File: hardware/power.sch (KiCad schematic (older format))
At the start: 51 parts, among them P1 CONN_01X02, Q1 DMG4712SSS, SW1 SPST, U7 LT3471, U8 PDM1-S

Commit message: Update sensors, hbridge caps, add heatsink
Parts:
- removed Q?: Q_NMOS_GDS, symbol Q_NMOS_GDS
- added C59: 1u, Capacitors_SMD:C_1206, symbol C
- added Q2: DMG4712SSS, symbol Q_NMOS_GDS
- added R42: 10k, symbol R
- C10, C11, C12, C7, C8, C9: footprint (none) -> Capacitors_SMD:C_0603
- C13, C14, C16, C4, C47, C48, C49: renamed from C?; footprint (none) -> Capacitors_SMD:C_0603
- C15: renamed from C?; footprint (none) -> Capacitors_SMD:C_1206
- C50: renamed from C?; value 10u -> 100n; footprint (none) -> Capacitors_SMD:C_1206
- R41: renamed from R?; value 10 -> 100
- gave numbers to parts that had none: 15
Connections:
- wire segments 123 -> 126

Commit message: Layout first draft
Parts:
- removed Q1, Q2: DMG4712SSS, symbol Q_NMOS_GDS
- added Q1, Q2: DMG4712SSS, Housings_SOIC:SOIC-8_3.9x4.9mm_Pitch1.27mm, symbol NMOS_8PIN
- R15: footprint (none) -> Resistors_SMD:R_0603
- U10: footprint (none) -> TO_SOT_Packages_SMD:TO-252-2Lead
- U16: footprint (none) -> TO_SOT_Packages_SMD:SOT-23-6
- U17, U9: footprint (none) -> TO_SOT_Packages_SMD:SOT-23-5
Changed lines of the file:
@@
-$EndComp
-$Comp
-L Q_NMOS_GDS Q1
-U 1 1 5987023F
-P 2100 7200
-F 0 "Q1" V 2100 7450 50  0000 R CNN
-F 1 "DMG4712SSS" V 2300 7450 50  0000 R CNN
-F 2 "" H 2300 7300 50  0001 C CNN
-F 3 "" H 2100 7200 50  0000 C CNN
-	1    2100 7200
-	0    -1   1    0
 $EndComp
 $Comp
@@
 F 0 "U16" H 6250 1500 60  0000 C CNN
 F 1 "MCP1501T-30E" H 6250 2050 60  0000 C CNN
-F 2 "" H 6200 1750 60  0001 C CNN
+F 2 "TO_SOT_Packages_SMD:SOT-23-6" H 6200 1750 60  0001 C CNN
 F 3 "" H 6200 1750 60  0000 C CNN
 	1    6250 1800
@@
 F 0 "U10" H 3800 1550 60  0000 C CNN
 F 1 "LF33ABDT" H 3650 1950 60  0000 C CNN
-F 2 "" H 3600 1600 60  0001 C CNN
+F 2 "TO_SOT_Packages_SMD:TO-252-2Lead" H 3600 1600 60  0001 C CNN
 F 3 "" H 3600 1600 60  0000 C CNN
 	1    3650 1750
@@
 F 0 "R15" V 2630 5850 50  0000 C CNN
 F 1 "10k" V 2550 5850 50  0000 C CNN
-F 2 "" V 2480 5850 50  0001 C CNN
+F 2 "Resistors_SMD:R_0603" V 2480 5850 50  0001 C CNN
 F 3 "" H 2550 5850 50  0000 C CNN
 	1    2550 5850
@@
 F 0 "U17" H 9250 4750 60  0000 C CNN
 F 1 "MIC5225-5.0" H 9300 5250 60  0000 C CNN
-F 2 "" H 9250 5000 60  0001 C CNN
+F 2 "TO_SOT_Packages_SMD:SOT-23-5" H 9250 5000 60  0001 C CNN
 F 3 "" H 9250 5000 60  0000 C CNN
 	1    9250 5000
@@
 F 0 "U9" H 3150 3050 60  0000 C CNN
 F 1 "MIC5225-5.0" H 3200 3550 60  0000 C CNN
-F 2 "" H 3150 3300 60  0001 C CNN
+F 2 "TO_SOT_Packages_SMD:SOT-23-5" H 3150 3300 60  0001 C CNN
 F 3 "" H 3150 3300 60  0000 C CNN
 	1    3150 3300
@@
 	9450 2000 9100 2000
 $Comp
-L Q_NMOS_GDS Q2
-U 1 1 59CA6F7C
-P 10050 2000
-F 0 "Q2" H 10300 2000 50  0000 R CNN
-F 1 "DMG4712SSS" H 10700 1900 50  0000 R CNN
-F 2 "" H 10250 2100 50  0001 C CNN
-F 3 "" H 10050 2000 50  0000 C CNN
-	1    10050 2000
-	1    0    0    -1
-$EndComp
-$Comp
 L R R42
 U 1 1 59CA88AD
@@
 	11000 2350 11000 1900
 Connection ~ 10750 2350
+$Comp
+L NMOS_8PIN Q2
+U 1 1 59BD8B92
+P 10050 2000
+F 0 "Q2" H 10350 2050 50  0000 R CNN
+F 1 "DMG4712SSS" H 10700 1950 50  0000 R CNN
+F 2 "Housings_SOIC:SOIC-8_3.9x4.9mm_Pitch1.27mm" H 10250 2100 50  0001 C CNN
+F 3 "" H 10050 2000 50  0000 C CNN
+	1    10050 2000
+	1    0    0    -1
+$EndComp
+$Comp
+L NMOS_8PIN Q1
+U 1 1 59BDA6D3
+P 2100 7200
+F 0 "Q1" V 2100 7450 50  0000 R CNN
+F 1 "DMG4712SSS" V 2350 7400 50  0000 R CNN
+F 2 "Housings_SOIC:SOIC-8_3.9x4.9mm_Pitch1.27mm" H 2300 7300 50  0001 C CNN
+F 3 "" H 2100 7200 50  0000 C CNN
+	1    2100 7200
+	0    -1   1    0
+$EndComp
 $EndSCHEMATC

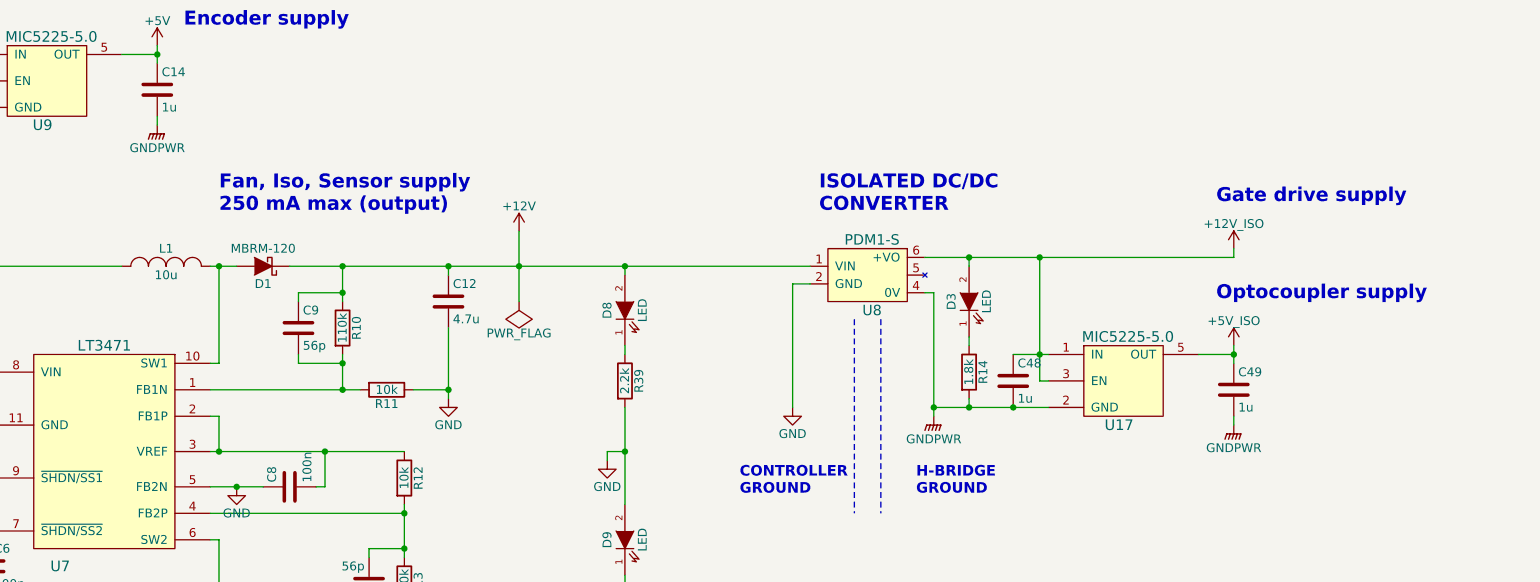
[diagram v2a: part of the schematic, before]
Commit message: revised power layout
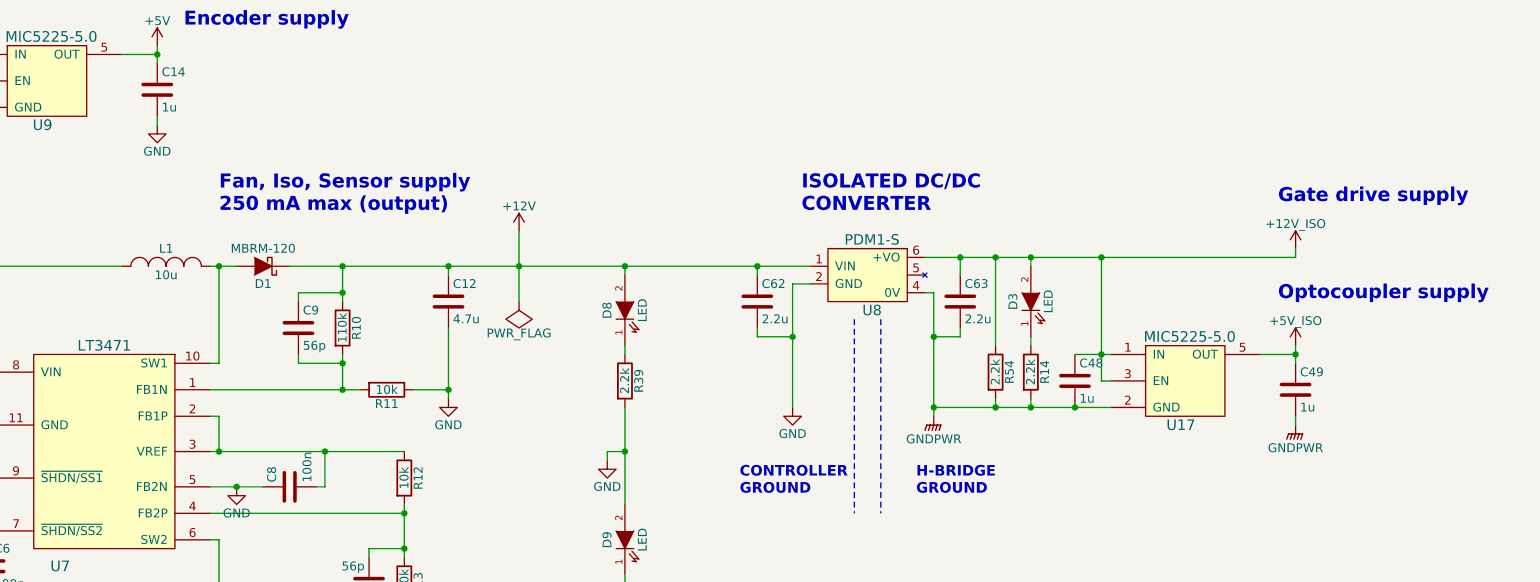
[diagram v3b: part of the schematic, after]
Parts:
- added C62, C63: 2.2u, symbol C
- added R54: 2.2k, symbol R
- R14: value 1.8k -> 2.2k
- U8: footprint (none) -> 2kwMotorController:PDM2-S
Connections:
- wire segments 126 -> 134
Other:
- moved on the sheet: C48, C49, D3, R14, U17
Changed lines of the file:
@@
 F 0 "U8" H 7850 4200 59  0000 C CNN
 F 1 "PDM1-S" H 7850 4600 59  0000 C CNN
-F 2 "" H 7850 4400 59  0001 C CNN
+F 2 "2kwMotorController:PDM2-S" H 7850 4400 59  0001 C CNN
 F 3 "" H 7850 4400 59  0000 C CNN
 	1    7800 4400
@@
 L R R14
 U 1 1 598583E6
-P 8400 4950
-F 0 "R14" V 8480 4950 50  0000 C CNN
-F 1 "1.8k" V 8400 4950 50  0000 C CNN
-F 2 "Resistors_SMD:R_0603" V 8330 4950 50  0001 C CNN
-F 3 "" H 8400 4950 50  0000 C CNN
-	1    8400 4950
+P 8750 4950
+F 0 "R14" V 8830 4950 50  0000 C CNN
+F 1 "2.2k" V 8750 4950 50  0000 C CNN
+F 2 "Resistors_SMD:R_0603" V 8680 4950 50  0001 C CNN
+F 3 "" H 8750 4950 50  0000 C CNN
+	1    8750 4950
 	1    0    0    -1
 $EndComp
@@
 L LED D3
 U 1 1 5985847D
-P 8400 4550
-F 0 "D3" H 8400 4650 50  0000 C CNN
-F 1 "LED" H 8400 4450 50  0000 C CNN
-F 2 "Diodes_SMD:SOD-123" H 8400 4550 50  0001 C CNN
-F 3 "" H 8400 4550 50  0000 C CNN
-	1    8400 4550
+P 8750 4550
+F 0 "D3" H 8750 4650 50  0000 C CNN
+F 1 "LED" H 8750 4450 50  0000 C CNN
+F 2 "Diodes_SMD:SOD-123" H 8750 4550 50  0001 C CNN
+F 3 "" H 8750 4550 50  0000 C CNN
+	1    8750 4550
 	0    -1   -1   0
 $EndComp
@@
 Text Notes 7100 5650 0    60   ~ 12
 CONTROLLER\nGROUND
-Text Notes 7550 4050 0    79   ~ 16
+Text Notes 7450 4050 0    79   ~ 16
 ISOLATED DC/DC\nCONVERTER
 $Comp
@@
 L +12V_ISO #PWR031
 U 1 1 59AAFB5D
-P 9900 4250
-F 0 "#PWR031" H 9900 4100 50  0001 C CNN
-F 1 "+12V_ISO" H 9900 4390 50  0000 C CNN
-F 2 "" H 9900 4250 50  0000 C CNN
-F 3 "" H 9900 4250 50  0000 C CNN
-	1    9900 4250
+P 10250 4250
+F 0 "#PWR031" H 10250 4100 50  0001 C CNN
+F 1 "+12V_ISO" H 10250 4390 50  0000 C CNN
+F 2 "" H 10250 4250 50  0000 C CNN
+F 3 "" H 10250 4250 50  0000 C CNN
+	1    10250 4250
 	1    0    0    -1
 $EndComp
@@
 L +5V_ISO #PWR041
 U 1 1 59B4088F
-P 9900 4800
-F 0 "#PWR041" H 9900 4650 50  0001 C CNN
-F 1 "+5V_ISO" H 9900 4940 50  0000 C CNN
-F 2 "" H 9900 4800 50  0000 C CNN
-F 3 "" H 9900 4800 50  0000 C CNN
-	1    9900 4800
+P 10250 4800
+F 0 "#PWR041" H 10250 4650 50  0001 C CNN
+F 1 "+5V_ISO" H 10250 4940 50  0000 C CNN
+F 2 "" H 10250 4800 50  0000 C CNN
+F 3 "" H 10250 4800 50  0000 C CNN
+	1    10250 4800
 	1    0    0    -1
 $EndComp
@@
 L GNDPWR #PWR042
 U 1 1 59B428AC
-P 9900 5250
-F 0 "#PWR042" H 9900 5050 50  0001 C CNN
-F 1 "GNDPWR" H 9900 5120 50  0000 C CNN
-F 2 "" H 9900 5200 50  0000 C CNN
-F 3 "" H 9900 5200 50  0000 C CNN
-	1    9900 5250
+P 10250 5250
+F 0 "#PWR042" H 10250 5050 50  0001 C CNN
+F 1 "GNDPWR" H 10250 5120 50  0000 C CNN
+F 2 "" H 10250 5200 50  0000 C CNN
+F 3 "" H 10250 5200 50  0000 C CNN
+	1    10250 5250
 	1    0    0    -1
 $EndComp
@@
 Text Notes 6650 6500 0    79   ~ 16
 Sensor supply\n60 mA max (output)
-Text Notes 9800 4550 0    79   ~ 16
+Text Notes 10150 4550 0    79   ~ 16
 Optocoupler supply
-Text Notes 9800 4000 0    79   ~ 16
+Text Notes 10150 4000 0    79   ~ 16
 Gate drive supply
 $Comp
@@
 L C C49
 U 1 1 59B42573
-P 9900 5050
-F 0 "C49" H 9925 5150 50  0000 L CNN
-F 1 "1u" H 9925 4950 50  0000 L CNN
-F 2 "Capacitors_SMD:C_0603" H 9938 4900 50  0001 C CNN
-F 3 "" H 9900 5050 50  0000 C CNN
-	1    9900 5050
+P 10250 5050
+F 0 "C49" H 10275 5150 50  0000 L CNN
+F 1 "1u" H 10275 4950 50  0000 L CNN
+F 2 "Capacitors_SMD:C_0603" H 10288 4900 50  0001 C CNN
+F 3 "" H 10250 5050 50  0000 C CNN
+	1    10250 5050
 	1    0    0    -1
 $EndComp
@@
 L C C48
 U 1 1 59BEDB92
-P 8650 5000
-F 0 "C48" H 8675 5100 50  0000 L CNN
-F 1 "1u" H 8675 4900 50  0000 L CNN
-F 2 "Capacitors_SMD:C_0603" H 8688 4850 50  0001 C CNN
-F 3 "" H 8650 5000 50  0000 C CNN
-	1    8650 5000
+P 9000 5000
+F 0 "C48" H 9025 5100 50  0000 L CNN
+F 1 "1u" H 9025 4900 50  0000 L CNN
+F 2 "Capacitors_SMD:C_0603" H 9038 4850 50  0001 C CNN
+F 3 "" H 9000 5000 50  0000 C CNN
+	1    9000 5000
 	1    0    0    -1
 $EndComp
@@
 L MIC5225-5.0 U17
 U 1 1 59BF0E85
-P 9250 5000
-F 0 "U17" H 9250 4750 60  0000 C CNN
-F 1 "MIC5225-5.0" H 9300 5250 60  0000 C CNN
-F 2 "TO_SOT_Packages_SMD:SOT-23-5" H 9250 5000 60  0001 C CNN
-F 3 "" H 9250 5000 60  0000 C CNN
-	1    9250 5000
-	1    0    0    -1
-$EndComp
-$Comp
-L GNDPWR #PWR045
-U 1 1 59BF2CFC
-P 3800 3550
-F 0 "#PWR045" H 3800 3350 50  0001 C CNN
-F 1 "GNDPWR" H 3800 3420 50  0000 C CNN
-F 2 "" H 3800 3500 50  0000 C CNN
-F 3 "" H 3800 3500 50  0000 C CNN
-	1    3800 3550
+P 9600 5000
+F 0 "U17" H 9600 4750 60  0000 C CNN
+F 1 "MIC5225-5.0" H 9650 5250 60  0000 C CNN
+F 2 "TO_SOT_Packages_SMD:SOT-23-5" H 9600 5000 60  0001 C CNN
+F 3 "" H 9600 5000 60  0000 C CNN
+	1    9600 5000
 	1    0    0    -1
 $EndComp
@@
 	2550 1350 2550 1250
 Wire Wire Line
-	8150 4300 9900 4300
-Connection ~ 8800 4300
+	8150 4300 10250 4300
+Connection ~ 9150 4300
 Wire Wire Line
 	8150 4500 8200 4500
@@
 	8200 4500 8200 5200
 Wire Wire Line
-	8400 4750 8400 4800
-Wire Wire Line
-	8400 5100 8400 5150
-Wire Wire Line
-	8200 5150 8850 5150
+	8750 4750 8750 4800
+Wire Wire Line
+	8750 5100 8750 5150
+Wire Wire Line
+	8200 5150 9200 5150
 Connection ~ 8200 5150
 Wire Wire Line
@@
 	7400 4450 7400 5150
 Wire Wire Line
-	8400 4350 8400 4300
-Connection ~ 8400 4300
+	8750 4350 8750 4300
+Connection ~ 8750 4300
 Wire Wire Line
 	1100 1450 1100 7350
@@
 Connection ~ 4250 5600
 Wire Wire Line
-	9900 4300 9900 4250
+	10250 4300 10250 4250
 Wire Wire Line
 	6700 1650 6950 1650
@@
 	5450 4400 5450 4350
 Wire Wire Line
-	8800 4300 8800 5000
-Wire Wire Line
-	8650 4850 8850 4850
-Wire Wire Line
-	8800 5000 8850 5000
-Connection ~ 8800 4850
-Connection ~ 8400 5150
-Wire Wire Line
-	9900 4800 9900 4900
-Wire Wire Line
-	9900 4850 9700 4850
-Wire Wire Line
-	9900 5250 9900 5200
-Connection ~ 9900 4850
+	9150 4300 9150 5000
+Wire Wire Line
+	9000 4850 9200 4850
+Wire Wire Line
+	9150 5000 9200 5000
+Connection ~ 9150 4850
+Connection ~ 8750 5150
+Wire Wire Line
+	10250 4800 10250 4900
+Wire Wire Line
+	10250 4850 10050 4850
+Wire Wire Line
+	10250 5250 10250 5200
+Connection ~ 10250 4850
 Wire Wire Line
 	4750 1700 4750 1650
@@
 Connection ~ 4850 4900
 Connection ~ 4850 4350
-Connection ~ 8650 5150
+Connection ~ 9000 5150
 Wire Wire Line
 	2700 3300 2750 3300
@@
 	0    -1   1    0
 $EndComp
+$Comp
+L C C62
+U 1 1 59BA3720
+P 7200 4550
+F 0 "C62" H 7225 4650 50  0000 L CNN
+F 1 "2.2u" H 7225 4450 50  0000 L CNN
+F 2 "" H 7238 4400 50  0001 C CNN
+F 3 "" H 7200 4550 50  0000 C CNN
+	1    7200 4550
+	1    0    0    -1
+$EndComp
+Wire Wire Line
+	7200 4400 7200 4350
+Connection ~ 7200 4350
+Wire Wire Line
+	7200 4700 7200 4750
+Wire Wire Line
+	7200 4750 7400 4750
+Connection ~ 7400 4750
+$Comp
+L C C63
+U 1 1 59BA475B
+P 8350 4550
+F 0 "C63" H 8375 4650 50  0000 L CNN
+F 1 "2.2u" H 8375 4450 50  0000 L CNN
+F 2 "" H 8388 4400 50  0001 C CNN
+F 3 "" H 8350 4550 50  0000 C CNN
+	1    8350 4550
+	1    0    0    -1
+$EndComp
+Wire Wire Line
+	8350 4400 8350 4300
+Connection ~ 8350 4300
+Wire Wire Line
+	8350 4700 8350 4750
+Wire Wire Line
+	8350 4750 8200 4750
+Connection ~ 8200 4750
+$Comp
+L R R54
+U 1 1 59BA7A13
+P 8550 4950
+F 0 "R54" V 8630 4950 50  0000 C CNN
+F 1 "2.2k" V 8550 4950 50  0000 C CNN
+F 2 "" V 8480 4950 50  0001 C CNN
+F 3 "" H 8550 4950 50  0000 C CNN
+	1    8550 4950
+	1    0    0    -1
+$EndComp
+Wire Wire Line
+	8550 4800 8550 4300
+Connection ~ 8550 4300
+Wire Wire Line
+	8550 5100 8550 5150
+Connection ~ 8550 5150
+$Comp
+L GND #PWR?
+U 1 1 59BAC5F2
+P 3800 3550
+F 0 "#PWR?" H 3800 3300 50  0001 C CNN
+F 1 "GND" H 3800 3400 50  0000 C CNN
+F 2 "" H 3800 3550 50  0000 C CNN
+F 3 "" H 3800 3550 50  0000 C CNN
+	1    3800 3550
+	1    0    0    -1
+$EndComp
 $EndSCHEMATC
